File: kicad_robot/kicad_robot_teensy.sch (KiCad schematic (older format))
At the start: 2 parts, among them U12->5 R-78E5.0-1.0

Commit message: mise à jour
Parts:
- added ALIM: Screw_Terminal_01x02, symbol Connector:Screw_Terminal_01x02
- added J_FTM->R_COD_1, J_FTM->R_COD_2, J_I2C->MULTIPLEX: Conn_01x04_Male, symbol Connector:Conn_01x04_Male
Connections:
- net ALIM_12V: now also ALIM.1 (Pin_1)
- net ALIM_5V: now also J_FTM->R_COD_1.1 (Pin_1), J_FTM->R_COD_2.1 (Pin_1), J_I2C->MULTIPLEX.1 (Pin_1)
- net GND: now also ALIM.2 (Pin_2), J_FTM->R_COD_1.2 (Pin_2), J_FTM->R_COD_2.2 (Pin_2), J_I2C->MULTIPLEX.2 (Pin_2)
- net I2C_SCLO: now also J_I2C->MULTIPLEX.4 (Pin_4)
- net I2C_SDAO: now also J_I2C->MULTIPLEX.3 (Pin_3)
- net BAR_MANCH_PWM renamed BAR_PWM
- net COULEUR_GPIO renamed COL_GPIO
- net FTM_1_phA renamed R_COD_1_phA
- net R_COD_1_phA: now also J_FTM->R_COD_1.3 (Pin_3)
- net FTM_1_phB renamed R_COD_1_phB
- net R_COD_1_phB: now also J_FTM->R_COD_1.4 (Pin_4)
- net FTM_2_phA renamed R_COD_2_phA
- net R_COD_2_phA: now also J_FTM->R_COD_2.3 (Pin_3)
- net FTM_2_phB renamed R_COD_2_phB
- net R_COD_2_phB: now also J_FTM->R_COD_2.4 (Pin_4)
- net LIDAR_PWM renamed LID_PWM
- net LIDAR_RX renamed LID_RX
- net LIDAR_TX renamed LID_TX
- net MOTEUR_1_PWM renamed MOT_1_PWM
- net MOTEUR_2_GPIO renamed MOT_2_DIR
- net Moteur_1_GPIO renamed MOT_1_DIR
- net Moteur_2_PWM renamed MOT_2_PWM
- net PAVILLON_PWM renamed PAV_PWM
- net TIRETTE_GPIO renamed TIR_GPIO
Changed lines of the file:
@@
 $EndComp
 Text GLabel 7450 2100 0    50   Input ~ 0
-LIDAR_RX
+LID_RX
 Text GLabel 7450 2200 0    50   Input ~ 0
-LIDAR_TX
+LID_TX
 Text GLabel 7450 2300 0    50   Input ~ 0
-LIDAR_PWM
+LID_PWM
 Text GLabel 7650 2800 0    50   Input ~ 0
 GPIO_DISPLAY_1
@@
 X-BEE_TX
 Text GLabel 7650 3500 0    50   Input ~ 0
-TIRETTE_GPIO
+TIR_GPIO
 $Comp
 L power:GND #PWR?
@@
 	10750 5500 10400 5500
 Text GLabel 7650 3600 0    50   Input ~ 0
-COULEUR_GPIO
+COL_GPIO
 Text GLabel 7450 4000 0    50   Input ~ 0
-FTM_2_phA
+R_COD_2_phA
 Text GLabel 7450 4100 0    50   Input ~ 0
-FTM_2_phB
+R_COD_2_phB
 Text GLabel 7700 4900 0    50   Input ~ 0
-Moteur_1_GPIO
+MOT_1_DIR
 Text GLabel 7700 5000 0    50   Input ~ 0
-MOTEUR_2_GPIO
+MOT_2_DIR
 Text GLabel 7700 5100 0    50   Input ~ 0
-Moteur_2_PWM
+MOT_2_PWM
 Text GLabel 7700 5200 0    50   Input ~ 0
-MOTEUR_1_PWM
+MOT_1_PWM
 Text GLabel 7700 5300 0    50   Input ~ 0
-PAVILLON_PWM
+PAV_PWM
 Text GLabel 7700 5400 0    50   Input ~ 0
-BAR_MANCH_PWM
+BAR_PWM
 Text GLabel 7750 6200 0    50   Input ~ 0
-FTM_1_phA
+R_COD_1_phA
 Text GLabel 7750 6300 0    50   Input ~ 0
-FTM_1_phB
+R_COD_1_phB
 Wire Wire Line
 	7750 6300 8100 6300
@@
 Wire Wire Line
 	7150 1000 7450 1000
+$Comp
+L Connector:Screw_Terminal_01x02 ALIM
+U 1 1 60342002
+P 10150 1050
+F 0 "ALIM" H 10230 1042 50  0000 L CNN
+F 1 "Screw_Terminal_01x02" H 10230 951 50  0000 L CNN
+F 2 "" H 10150 1050 50  0001 C CNN
+F 3 "~" H 10150 1050 50  0001 C CNN
+	1    10150 1050
+	1    0    0    -1
+$EndComp
+Text GLabel 9750 1050 0    50   Input ~ 0
+ALIM_12V
+$Comp
+L power:GND #PWR?
+U 1 1 60342E59
+P 9750 1150
+F 0 "#PWR?" H 9750 900 50  0001 C CNN
+F 1 "GND" H 9755 977 50  0000 C CNN
+F 2 "" H 9750 1150 50  0001 C CNN
+F 3 "" H 9750 1150 50  0001 C CNN
+	1    9750 1150
+	0    1    1    0
+$EndComp
+Wire Wire Line
+	9750 1150 9950 1150
+Wire Wire Line
+	9750 1050 9950 1050
+$Comp
+L Connector:Conn_01x04_Male J_I2C->MULTIPLEX
+U 1 1 60344D96
+P 6750 800
+F 0 "J_I2C->MULTIPLEX" H 6722 682 50  0000 R CNN
+F 1 "Conn_01x04_Male" H 6722 773 50  0000 R CNN
+F 2 "" H 6750 800 50  0001 C CNN
+F 3 "~" H 6750 800 50  0001 C CNN
+	1    6750 800
+	-1   0    0    1
+$EndComp
+$Comp
+L power:GND #PWR?
+U 1 1 6034965D
+P 6400 800
+F 0 "#PWR?" H 6400 550 50  0001 C CNN
+F 1 "GND" H 6405 627 50  0000 C CNN
+F 2 "" H 6400 800 50  0001 C CNN
+F 3 "" H 6400 800 50  0001 C CNN
+	1    6400 800
+	0    1    1    0
+$EndComp
+Text GLabel 6400 900  0    50   Input ~ 0
+ALIM_5V
+Text GLabel 6400 700  0    50   Input ~ 0
+I2C_SDAO
+Text GLabel 6400 600  0    50   Input ~ 0
+I2C_SCLO
+Wire Wire Line
+	6400 600  6550 600
+Wire Wire Line
+	6400 700  6550 700
+Wire Wire Line
+	6400 800  6550 800
+Wire Wire Line
+	6400 900  6550 900
+$Comp
+L Connector:Conn_01x04_Male J_FTM->R_COD_1
+U 1 1 6034C8A3
+P 6750 1350
+F 0 "J_FTM->R_COD_1" H 6722 1232 50  0000 R CNN
+F 1 "Conn_01x04_Male" H 6722 1323 50  0000 R CNN
+F 2 "" H 6750 1350 50  0001 C CNN
+F 3 "~" H 6750 1350 50  0001 C CNN
+	1    6750 1350
+	-1   0    0    1
+$EndComp
+Text GLabel 6400 1450 0    50   Input ~ 0
+ALIM_5V
+$Comp
+L power:GND #PWR?
+U 1 1 6034D5A6
+P 6400 1350
+F 0 "#PWR?" H 6400 1100 50  0001 C CNN
+F 1 "GND" H 6405 1177 50  0000 C CNN
+F 2 "" H 6400 1350 50  0001 C CNN
+F 3 "" H 6400 1350 50  0001 C CNN
+	1    6400 1350
+	0    1    1    0
+$EndComp
+Text GLabel 6400 1250 0    50   Input ~ 0
+R_COD_1_phA
+Text GLabel 6400 1150 0    50   Input ~ 0
+R_COD_1_phB
+Wire Wire Line
+	6400 1150 6550 1150
+Wire Wire Line
+	6550 1250 6400 1250
+Wire Wire Line
+	6400 1350 6550 1350
+Wire Wire Line
+	6550 1450 6400 1450
+$Comp
+L Connector:Conn_01x04_Male J_FTM->R_COD_2
+U 1 1 6035325F
+P 6800 1950
+F 0 "J_FTM->R_COD_2" H 6772 1832 50  0000 R CNN
+F 1 "Conn_01x04_Male" H 6772 1923 50  0000 R CNN
+F 2 "" H 6800 1950 50  0001 C CNN
+F 3 "~" H 6800 1950 50  0001 C CNN
+	1    6800 1950
+	-1   0    0    1
+$EndComp
+Text GLabel 6450 2050 0    50   Input ~ 0
+ALIM_5V
+$Comp
+L power:GND #PWR?
+U 1 1 60353D5D
+P 6450 1950
+F 0 "#PWR?" H 6450 1700 50  0001 C CNN
+F 1 "GND" H 6455 1777 50  0000 C CNN
+F 2 "" H 6450 1950 50  0001 C CNN
+F 3 "" H 6450 1950 50  0001 C CNN
+	1    6450 1950
+	0    1    1    0
+$EndComp
+Text GLabel 6450 1850 0    50   Input ~ 0
+R_COD_2_phA
+Text GLabel 6450 1750 0    50   Input ~ 0
+R_COD_2_phB
+Wire Wire Line
+	6450 1750 6600 1750
+Wire Wire Line
+	6600 1850 6450 1850
+Wire Wire Line
+	6450 1950 6600 1950
+Wire Wire Line
+	6600 2050 6450 2050
 $EndSCHEMATC

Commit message: MAJ
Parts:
- added CONN_COL, CONN_TIR: Conn_01x02_Male, symbol Connector:Conn_01x02_Male
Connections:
- net COL_GPIO: now also CONN_COL.1 (Pin_1)
- net GND: now also CONN_COL.2 (Pin_2), CONN_TIR.2 (Pin_2)
- net TIR_GPIO: now also CONN_TIR.1 (Pin_1)
- net ALIM_12V renamed +12V
- net ALIM_5V renamed +5V
- net BAR_PWM renamed BAR_SERV
- net PAV_PWM renamed PAV_SERV
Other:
- moved on the sheet: ALIM, J_FTM->R_COD_1, J_FTM->R_COD_2, J_I2C->MULTIPLEX, U12->5, U?

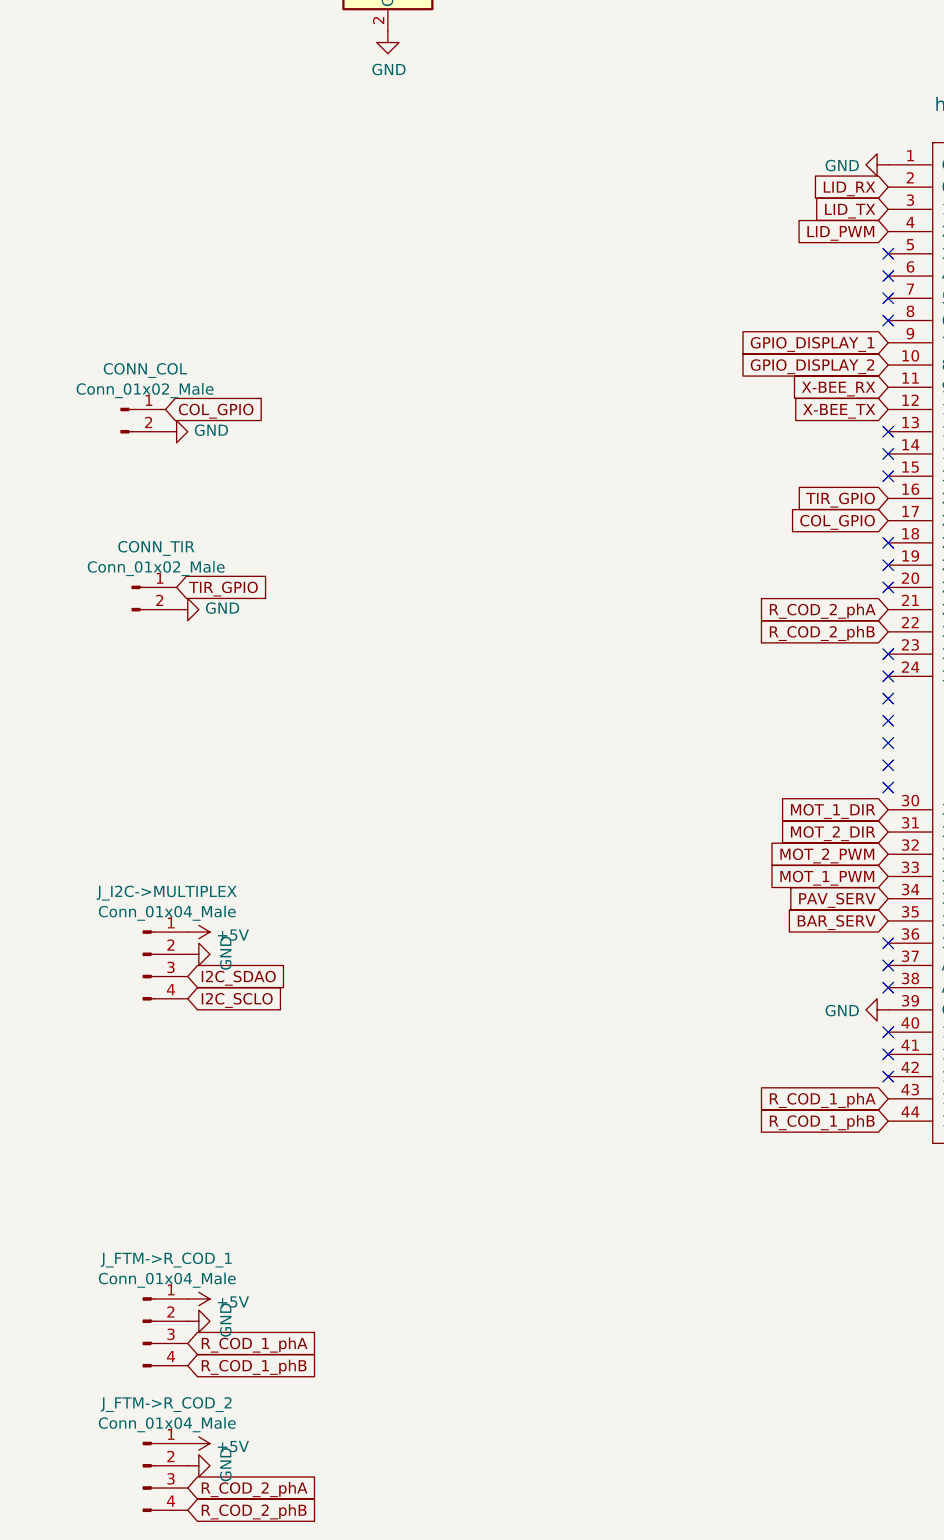
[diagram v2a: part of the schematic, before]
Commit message: Ajout des derniers composants
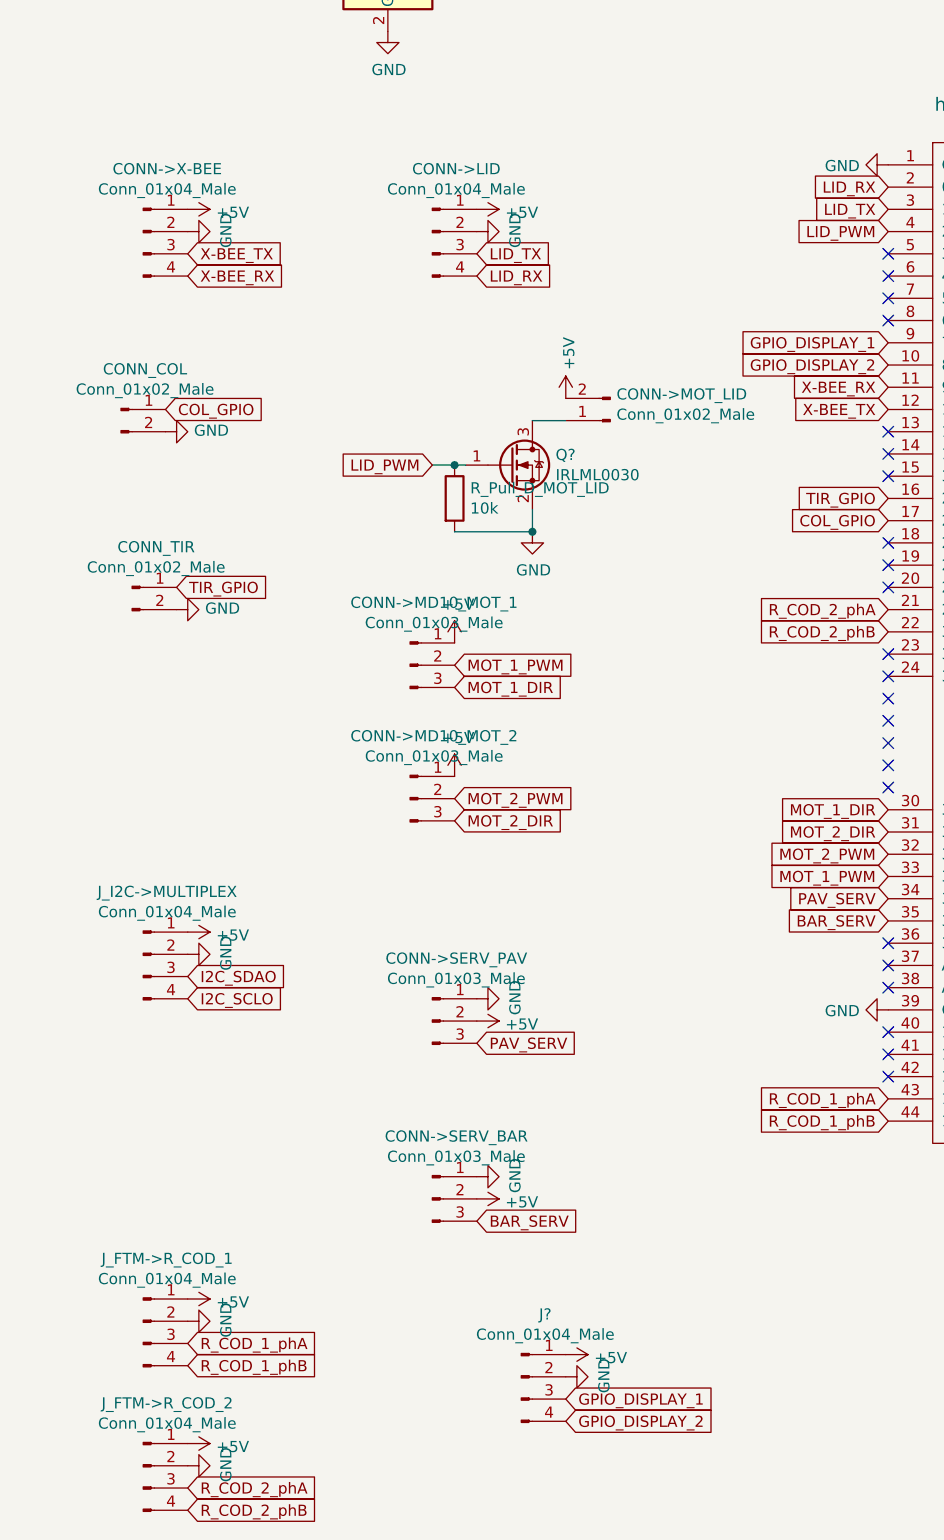
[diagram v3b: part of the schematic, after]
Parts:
- added CONN->LID, CONN->X-BEE, J?: Conn_01x04_Male, symbol Connector:Conn_01x04_Male
- added CONN->MD10_MOT_1, CONN->MD10_MOT_2, CONN->SERV_BAR, CONN->SERV_PAV: Conn_01x03_Male, symbol Connector:Conn_01x03_Male
- added CONN->MOT_LID: Conn_01x02_Male, symbol Connector:Conn_01x02_Male
- added Q?: IRLML0030, Package_TO_SOT_SMD:SOT-23, symbol Transistor_FET:IRLML0030
- added R_Pull_D_MOT_LID: 10k, symbol Device:R
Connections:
- net +5V: now also CONN->LID.1 (Pin_1), CONN->MD10_MOT_1.1 (Pin_1), CONN->MD10_MOT_2.1 (Pin_1), CONN->MOT_LID.2 (Pin_2), CONN->SERV_BAR.2 (Pin_2), CONN->SERV_PAV.2 (Pin_2), CONN->X-BEE.1 (Pin_1), J?.1 (Pin_1)
- net BAR_SERV: now also CONN->SERV_BAR.3 (Pin_3)
- net GND: now also CONN->LID.2 (Pin_2), CONN->SERV_BAR.1 (Pin_1), CONN->SERV_PAV.1 (Pin_1), CONN->X-BEE.2 (Pin_2), J?.2 (Pin_2), Q?.2 (S), R_Pull_D_MOT_LID.2
- net GPIO_DISPLAY_1: now also J?.3 (Pin_3)
- net GPIO_DISPLAY_2: now also J?.4 (Pin_4)
- net LID_PWM: now also Q?.1 (G), R_Pull_D_MOT_LID.1
- net LID_RX: now also CONN->LID.4 (Pin_4)
- net LID_TX: now also CONN->LID.3 (Pin_3)
- net MOT_1_DIR: now also CONN->MD10_MOT_1.3 (Pin_3)
- net MOT_1_PWM: now also CONN->MD10_MOT_1.2 (Pin_2)
- net MOT_2_DIR: now also CONN->MD10_MOT_2.3 (Pin_3)
- net MOT_2_PWM: now also CONN->MD10_MOT_2.2 (Pin_2)
- net PAV_SERV: now also CONN->SERV_PAV.3 (Pin_3)
- net X-BEE_RX: now also CONN->X-BEE.4 (Pin_4)
- net X-BEE_TX: now also CONN->X-BEE.3 (Pin_3)
- new net: CONN->MOT_LID.1 (Pin_1), Q?.3 (D)

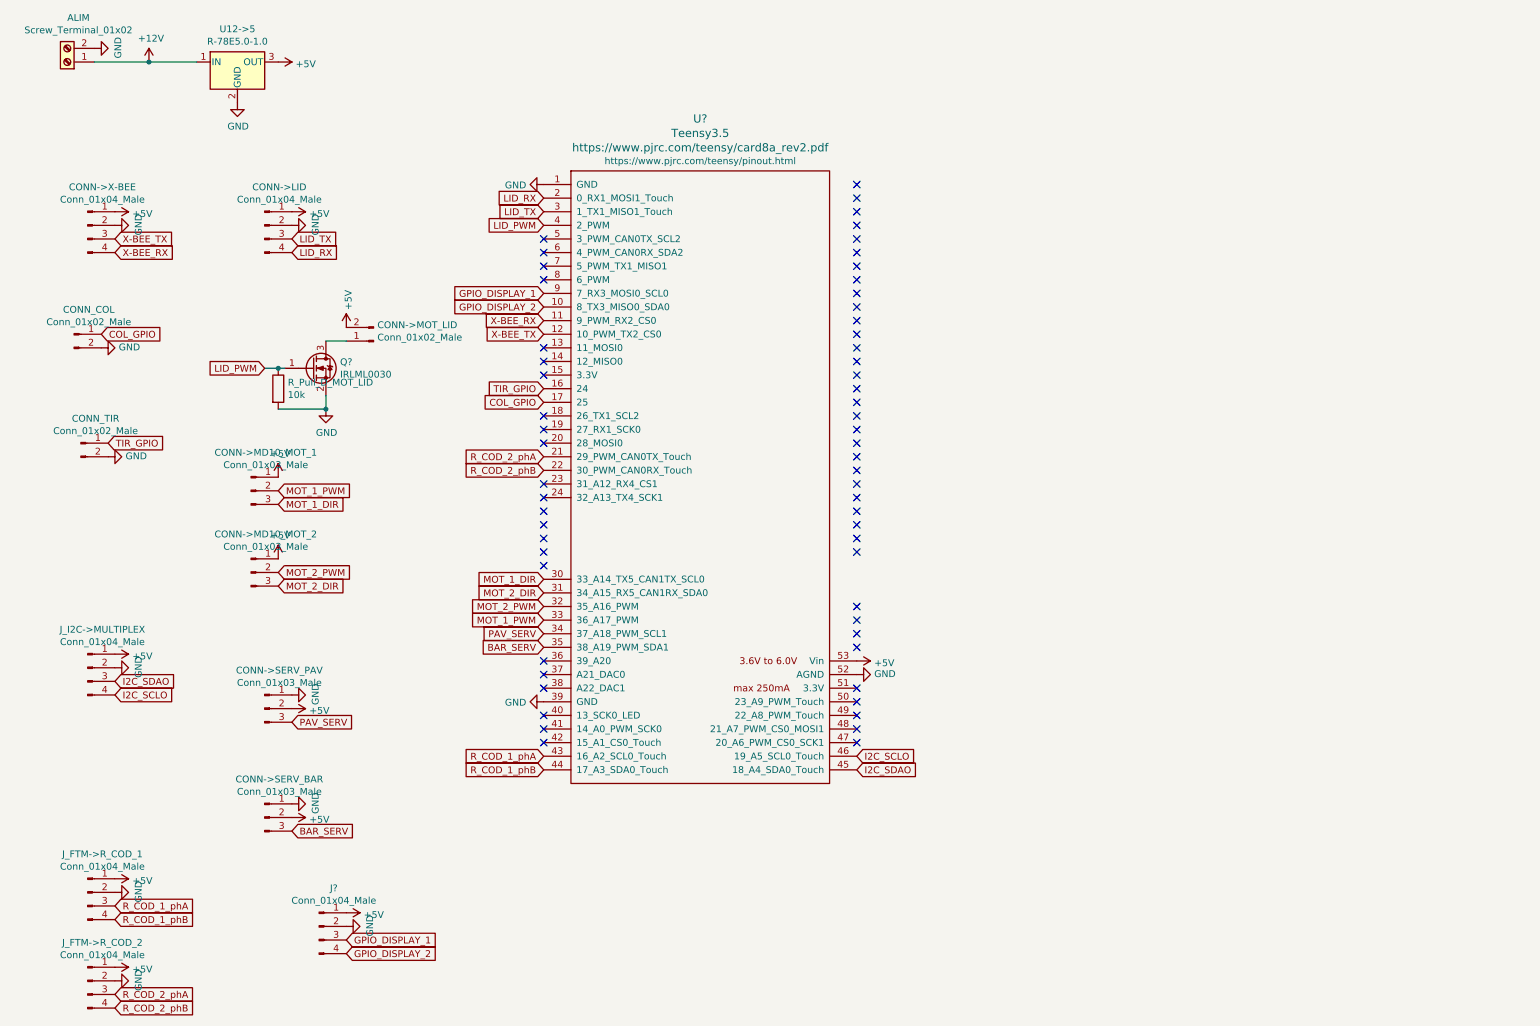
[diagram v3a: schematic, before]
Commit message: Ajout des footprint carte teensy
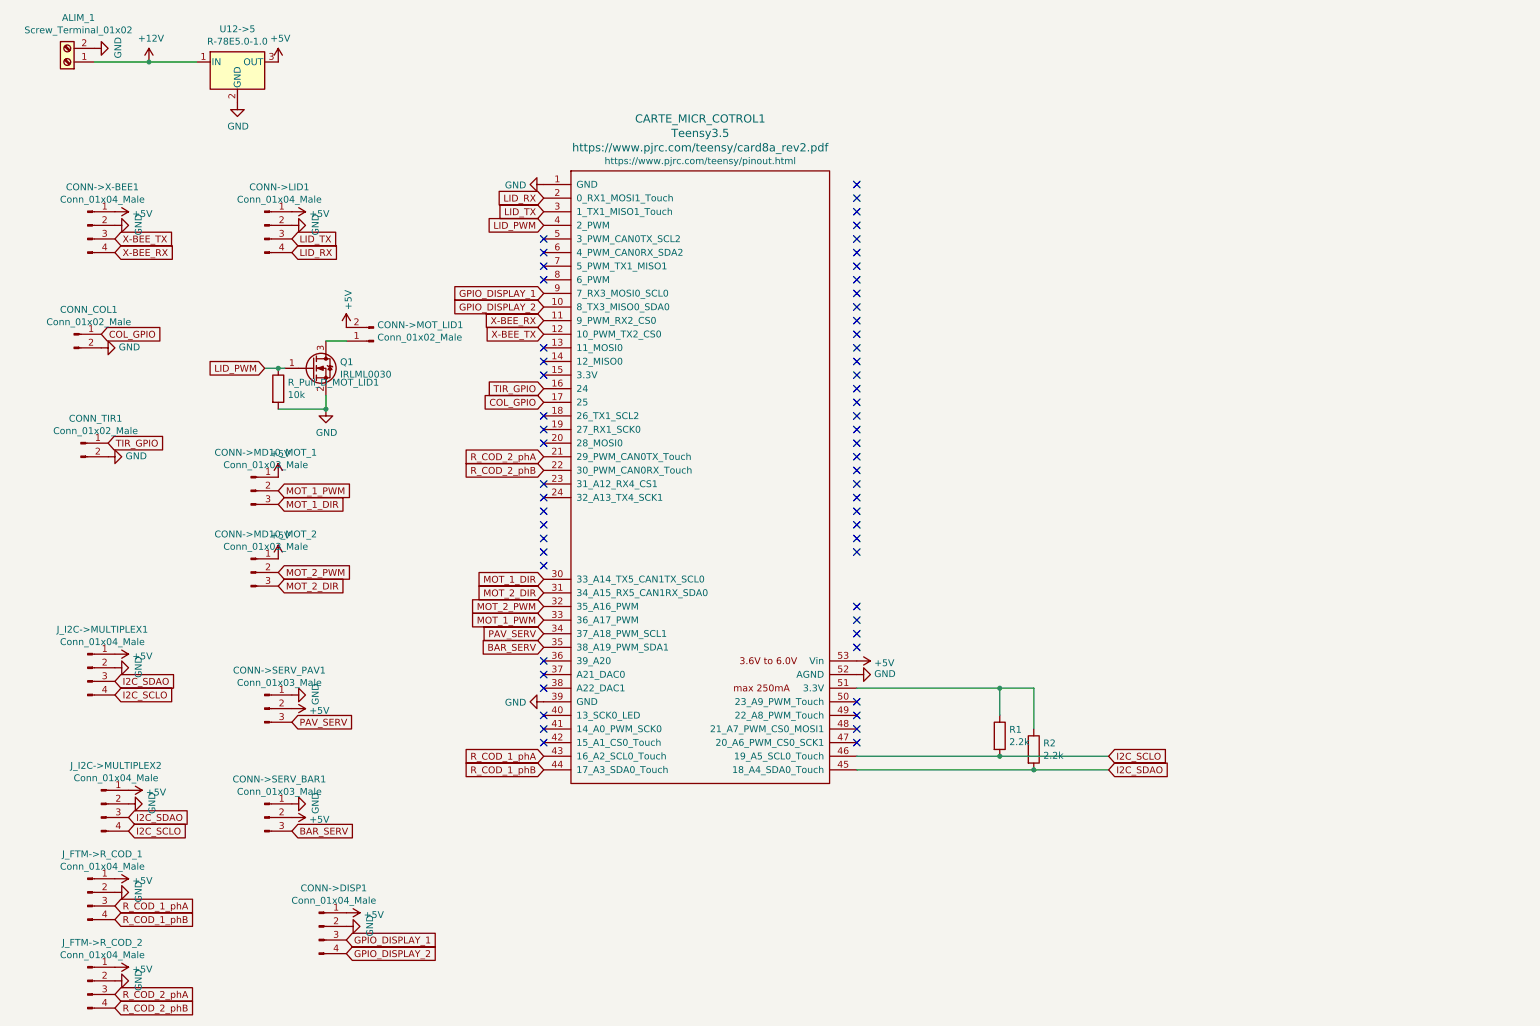
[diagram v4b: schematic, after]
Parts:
- added J_I2C->MULTIPLEX2: Conn_01x04_Male, Connector_JST:JST_XH_B4B-XH-A_1x04_P2.50mm_Vertical, symbol Connector:Conn_01x04_Male
- added R1, R2: 2.2k, Resistor_SMD:R_0603_1608Metric_Pad0.98x0.95mm_HandSolder, symbol Device:R
- ALIM_1: renamed from ALIM; footprint (none) -> TerminalBlock:TerminalBlock_bornier-2_P5.08mm
- CARTE_MICR_COTROL1: renamed from U?; footprint (none) -> teensy:Teensy35_36
- CONN->DISP1: renamed from J?; footprint (none) -> Connector_JST:JST_XH_B4B-XH-A_1x04_P2.50mm_Vertical
- CONN->LID1: renamed from CONN->LID; footprint (none) -> Connector_JST:JST_XH_B4B-XH-A_1x04_P2.50mm_Vertical
- CONN->MD10_MOT_1, CONN->MD10_MOT_2: footprint (none) -> Connector_JST:JST_XH_B3B-XH-A_1x03_P2.50mm_Vertical
- CONN->MOT_LID1: renamed from CONN->MOT_LID; footprint (none) -> Connector_JST:JST_XH_B2B-XH-A_1x02_P2.50mm_Vertical
- CONN->SERV_BAR1: renamed from CONN->SERV_BAR; footprint (none) -> Connector_PinHeader_2.54mm:PinHeader_1x03_P2.54mm_Vertical
- CONN->SERV_PAV1: renamed from CONN->SERV_PAV; footprint (none) -> Connector_PinHeader_2.54mm:PinHeader_1x03_P2.54mm_Vertical
- CONN->X-BEE1: renamed from CONN->X-BEE; footprint (none) -> Connector_JST:JST_XH_B4B-XH-A_1x04_P2.50mm_Vertical
- CONN_COL1: renamed from CONN_COL; footprint (none) -> Connector_JST:JST_XH_B2B-XH-A_1x02_P2.50mm_Vertical
- CONN_TIR1: renamed from CONN_TIR; footprint (none) -> Connector_JST:JST_XH_B2B-XH-A_1x02_P2.50mm_Vertical
- J_FTM->R_COD_1, J_FTM->R_COD_2: footprint (none) -> Connector_JST:JST_XH_B4B-XH-A_1x04_P2.50mm_Vertical
- J_I2C->MULTIPLEX1: renamed from J_I2C->MULTIPLEX; footprint (none) -> Connector_JST:JST_XH_B4B-XH-A_1x04_P2.50mm_Vertical
- R_Pull_D_MOT_LID1: renamed from R_Pull_D_MOT_LID; footprint (none) -> Resistor_SMD:R_0603_1608Metric_Pad0.98x0.95mm_HandSolder
- gave numbers to parts that had none: 1
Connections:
- net +5V: now also J_I2C->MULTIPLEX2.1 (Pin_1)
- net GND: now also J_I2C->MULTIPLEX2.2 (Pin_2)
- net I2C_SCLO: now also J_I2C->MULTIPLEX2.4 (Pin_4), R1.2
- net I2C_SDAO: now also J_I2C->MULTIPLEX2.3 (Pin_3), R2.2
- net at CARTE_MICR_COTROL1.51 (3.3V): now also R1.1, R2.1
- no-connect marks 60 -> 59
